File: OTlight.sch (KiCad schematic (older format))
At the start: 51 parts

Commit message: Everything Connected
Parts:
- removed P?: Vin, Pin_Headers:Pin_Header_Straight_1x02, symbol CONN_01X02
- removed P?: Vout, Pin_Headers:Pin_Header_Straight_1x02, symbol CONN_01X02
- added P1: CONN_01X01, symbol CONN_01X01
- gave numbers to parts that had none: 49
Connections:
- wire segments 228 -> 239
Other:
- note added: "ESPain"
- moved on the sheet: C1, C4, C6, R7

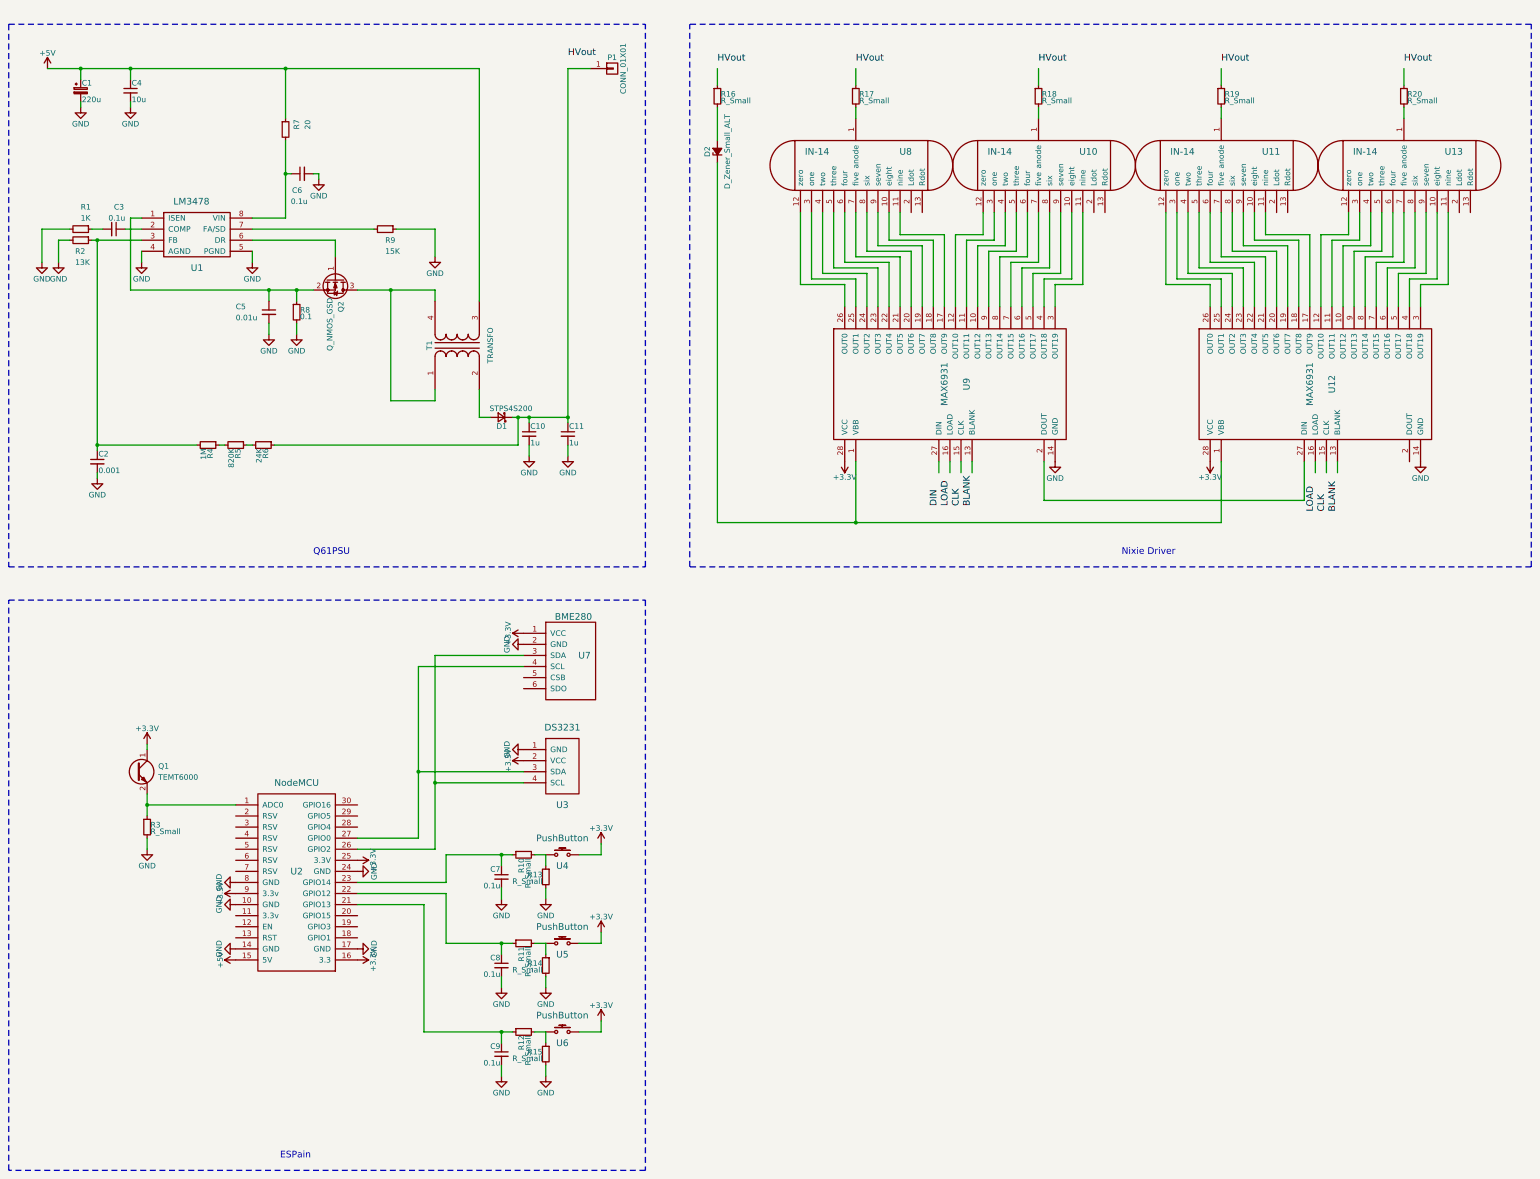
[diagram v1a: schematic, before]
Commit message: Touch up + added I2C Pullups
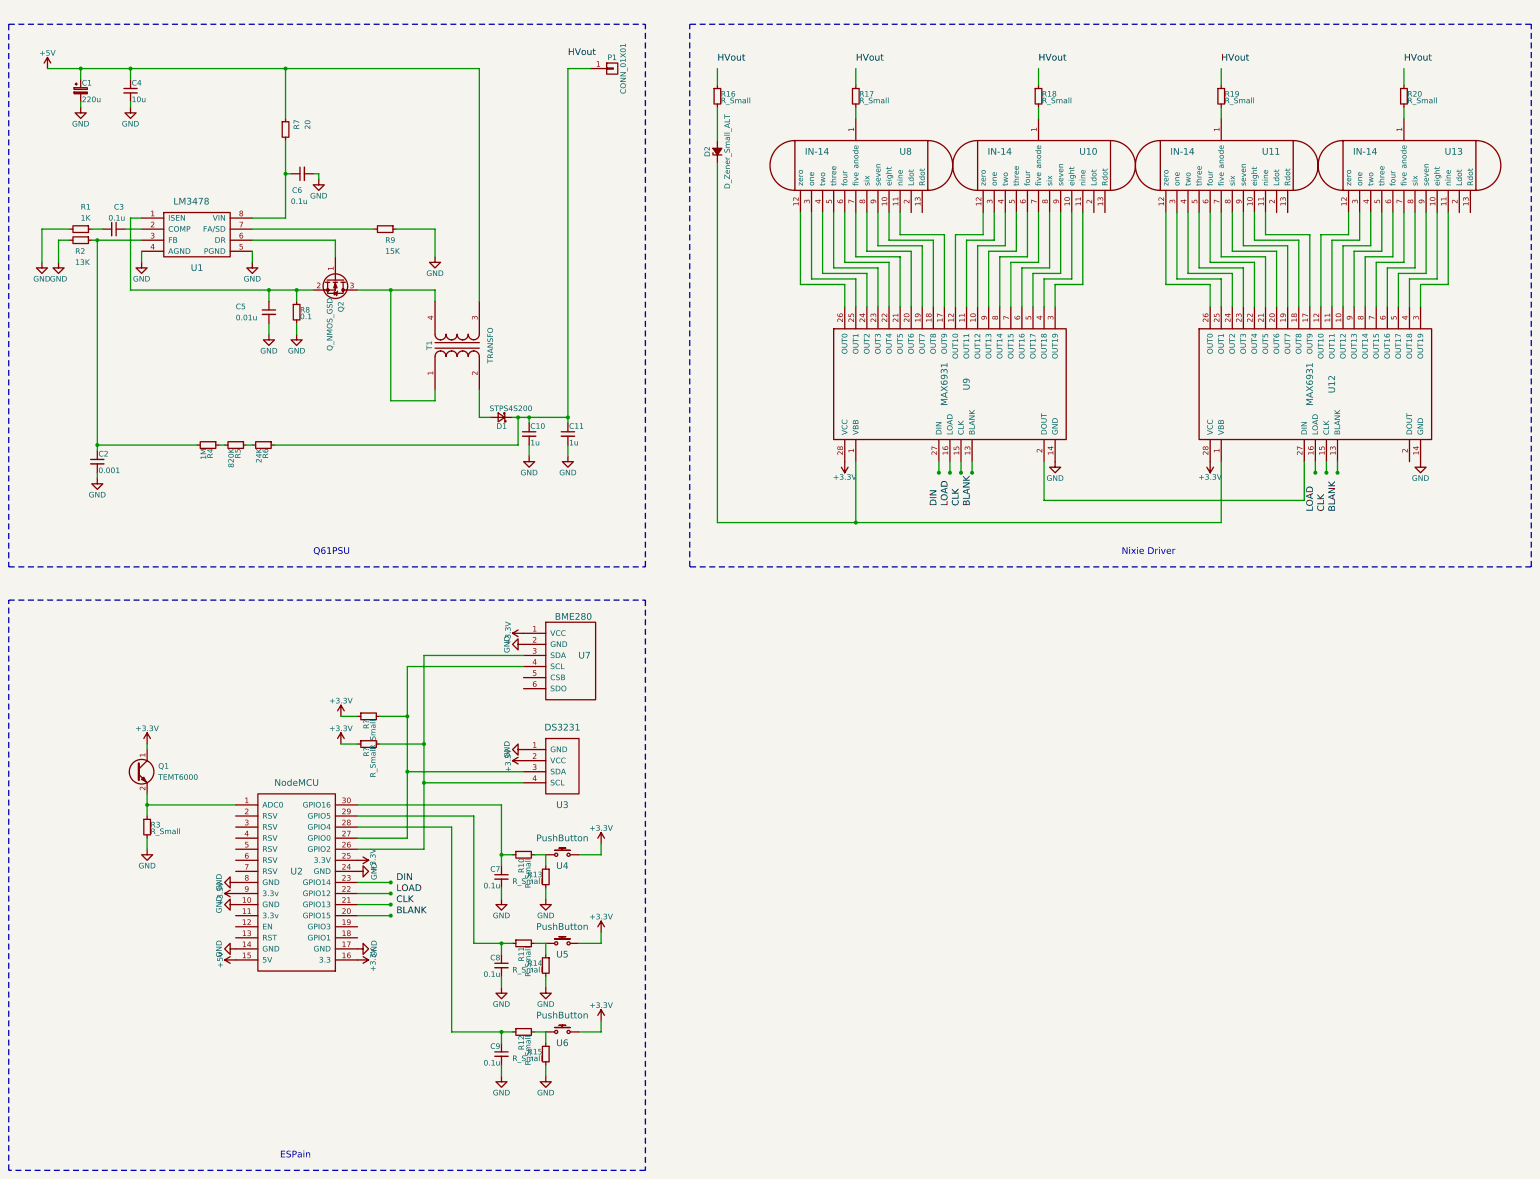
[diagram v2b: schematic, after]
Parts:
- added R? (x2): R_Small, symbol R_Small
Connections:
- wire segments 239 -> 267
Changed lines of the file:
@@
 LIBS:contrib
 LIBS:valves
+LIBS:ESP8266
 LIBS:bambouLab
-LIBS:ESP8266
 LIBS:OTlight-cache
 EELAYER 25 0
@@
 encoding utf-8
 Sheet 1 1
-Title ""
-Date ""
-Rev ""
-Comp ""
+Title "OT;Light"
+Date "2017-01-21"
+Rev "0.1"
+Comp "bambou;Lab"
 Comment1 ""
 Comment2 ""
@@
 Connection ~ 1800 1050
 Wire Wire Line
-	3200 1700 3200 2400
+	3200 1700 3200 2000
+Wire Wire Line
+	3200 2000 3200 2400
 Wire Wire Line
 	3200 2000 3250 2000
@@
 	3650 2600 3650 2750
 Wire Wire Line
-	3850 3050 4550 3050
+	3850 3050 4150 3050
+Wire Wire Line
+	4150 3050 4550 3050
 Wire Wire Line
 	4150 3050 4150 4050
@@
 Connection ~ 4150 3050
 Wire Wire Line
-	1800 3050 3450 3050
+	1800 3050 3050 3050
+Wire Wire Line
+	3050 3050 3300 3050
+Wire Wire Line
+	3300 3050 3450 3050
 Wire Wire Line
 	3050 3050 3050 3150
@@
 	1550 2500 1450 2500
 Wire Wire Line
-	1450 2600 1900 2600
+	1450 2600 1500 2600
+Wire Wire Line
+	1500 2600 1900 2600
 Wire Wire Line
 	1250 2600 1150 2600
@@
 	5950 1050 5750 1050
 Wire Wire Line
-	5750 1050 5750 4250
-Wire Wire Line
-	5250 4200 5750 4200
+	5750 1050 5750 4200
+Wire Wire Line
+	5750 4200 5750 4250
+Wire Wire Line
+	5250 4200 5300 4200
+Wire Wire Line
+	5300 4200 5400 4200
+Wire Wire Line
+	5400 4200 5750 4200
 Wire Wire Line
 	4950 4200 5050 4200
@@
 Connection ~ 5400 4200
 Wire Wire Line
-	1500 2600 1500 4500
+	1500 2600 1500 4450
+Wire Wire Line
+	1500 4450 1500 4500
 Connection ~ 1500 2600
 Wire Wire Line
@@
 	7100 1900 7100 5150
 Wire Wire Line
-	7100 5150 11650 5150
+	7100 5150 8350 5150
+Wire Wire Line
+	8350 5150 11650 5150
 Wire Wire Line
 	8350 5150 8350 4600
@@
 	2750 7700 1950 7700
 Wire Wire Line
-	1950 7600 1950 7800
+	1950 7600 1950 7700
+Wire Wire Line
+	1950 7700 1950 7800
 $Comp
 L R_Small R3
@@
 	5550 8450 5550 8550
 Wire Wire Line
-	4650 8150 5250 8150
+	5150 7700 5150 8150
 Wire Wire Line
 	5150 8150 5150 8250
@@
 	5550 9250 5550 9350
 Wire Wire Line
-	4650 8950 5250 8950
-Wire Wire Line
 	5150 8950 5150 9050
 Wire Wire Line
@@
 	5550 10050 5550 10150
 Wire Wire Line
-	4450 9750 5250 9750
-Wire Wire Line
 	5150 9750 5150 9850
 Wire Wire Line
@@
 	3200 2400 2900 2400
 Wire Wire Line
-	4950 1050 1050 1050
+	1050 1050 1350 1050
+Wire Wire Line
+	1350 1050 1800 1050
+Wire Wire Line
+	1800 1050 3200 1050
+Wire Wire Line
+	3200 1050 4950 1050
 Text Notes 3150 10900 0    60   ~ 0
 ESPain
 Wire Wire Line
-	3850 8000 4400 8000
-Wire Wire Line
-	4400 8000 4400 6450
-Wire Wire Line
-	4400 6450 5350 6450
-Wire Wire Line
-	3850 8100 4550 8100
-Wire Wire Line
-	4550 8100 4550 6350
-Wire Wire Line
-	4550 6350 5350 6350
-Wire Wire Line
-	5350 7400 4400 7400
-Connection ~ 4400 7400
-Wire Wire Line
-	5350 7500 4550 7500
-Connection ~ 4550 7500
-Wire Wire Line
-	3850 8400 4650 8400
-Wire Wire Line
-	4650 8400 4650 8150
+	4300 8000 3850 8000
+Wire Wire Line
+	4300 6450 4300 6900
+Wire Wire Line
+	4300 6900 4300 7400
+Wire Wire Line
+	4300 7400 4300 8000
+Wire Wire Line
+	4300 6450 5350 6450
+Wire Wire Line
+	4450 8100 3850 8100
+Wire Wire Line
+	4450 6350 4450 7150
+Wire Wire Line
+	4450 7150 4450 7500
+Wire Wire Line
+	4450 7500 4450 8100
+Wire Wire Line
+	4450 6350 5350 6350
+Wire Wire Line
+	5350 7400 4300 7400
+Connection ~ 4300 7400
+Wire Wire Line
+	5350 7500 4450 7500
+Connection ~ 4450 7500
 Connection ~ 5150 8150
-Wire Wire Line
-	3850 8500 4650 8500
-Wire Wire Line
-	4650 8500 4650 8950
 Connection ~ 5150 8950
-Wire Wire Line
-	3850 8600 4450 8600
-Wire Wire Line
-	4450 8600 4450 9750
 Connection ~ 5150 9750
+Wire Wire Line
+	3850 7700 5150 7700
+Wire Wire Line
+	5150 8150 5250 8150
+Wire Wire Line
+	3850 7800 4900 7800
+Wire Wire Line
+	3850 7900 4700 7900
+Wire Wire Line
+	4900 8950 5150 8950
+Wire Wire Line
+	5150 8950 5250 8950
+Wire Wire Line
+	4900 7800 4900 8950
+Wire Wire Line
+	3850 8400 4150 8400
+Wire Wire Line
+	3850 8500 4150 8500
+Wire Wire Line
+	3850 8600 4150 8600
+Wire Wire Line
+	3850 8700 4150 8700
+Text Label 4200 8400 0    60   ~ 0
+DIN
+Text Label 4200 8500 0    60   ~ 0
+LOAD
+Text Label 4200 8600 0    60   ~ 0
+CLK
+Text Label 4200 8700 0    60   ~ 0
+BLANK
+Connection ~ 4150 8400
+Connection ~ 4150 8500
+Connection ~ 4150 8600
+Connection ~ 4150 8700
+Connection ~ 9100 4700
+Connection ~ 9200 4700
+Connection ~ 9300 4700
+Connection ~ 9400 4700
+Connection ~ 12500 4700
+Connection ~ 12600 4700
+Connection ~ 12700 4700
+Wire Wire Line
+	4700 7900 4700 9750
+Wire Wire Line
+	4700 9750 5150 9750
+Wire Wire Line
+	5150 9750 5250 9750
+$Comp
+L +3.3V #PWR?
+U 1 1 5884F76D
+P 3700 6900
+F 0 "#PWR?" H 3700 6750 50  0001 C CNN
+F 1 "+3.3V" H 3700 7040 50  0000 C CNN
+F 2 "" H 3700 6900 50  0000 C CNN
+F 3 "" H 3700 6900 50  0000 C CNN
+	1    3700 6900
+	-1   0    0    -1
+$EndComp
+$Comp
+L +3.3V #PWR?
+U 1 1 5884F80E
+P 3700 7150
+F 0 "#PWR?" H 3700 7000 50  0001 C CNN
+F 1 "+3.3V" H 3700 7290 50  0000 C CNN
+F 2 "" H 3700 7150 50  0000 C CNN
+F 3 "" H 3700 7150 50  0000 C CNN
+	1    3700 7150
+	-1   0    0    -1
+$EndComp
+$Comp
+L R_Small R?
+U 1 1 5884F8AF
+P 3950 6900
+F 0 "R?" H 3980 6920 50  0000 L CNN
+F 1 "R_Small" H 3980 6860 50  0000 L CNN
+F 2 "" H 3950 6900 50  0000 C CNN
+F 3 "" H 3950 6900 50  0000 C CNN
+	1    3950 6900
+	0    -1   1    0
+$EndComp
+$Comp
+L R_Small R?
+U 1 1 5884F982
+P 3950 7150
+F 0 "R?" H 3980 7170 50  0000 L CNN
+F 1 "R_Small" H 3980 7110 50  0000 L CNN
+F 2 "" H 3950 7150 50  0000 C CNN
+F 3 "" H 3950 7150 50  0000 C CNN
+	1    3950 7150
+	0    -1   1    0
+$EndComp
+Wire Wire Line
+	3700 6900 3850 6900
+Wire Wire Line
+	3850 7150 3700 7150
+Wire Wire Line
+	4050 6900 4300 6900
+Connection ~ 4300 6900
+Wire Wire Line
+	4050 7150 4450 7150
+Connection ~ 4450 7150
 $EndSCHEMATC

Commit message: Schematic Update
changelog:
- Linked labels
- Added MAXIM6920 to rout the dot
- Set values to passive components
- Cosmetic changes
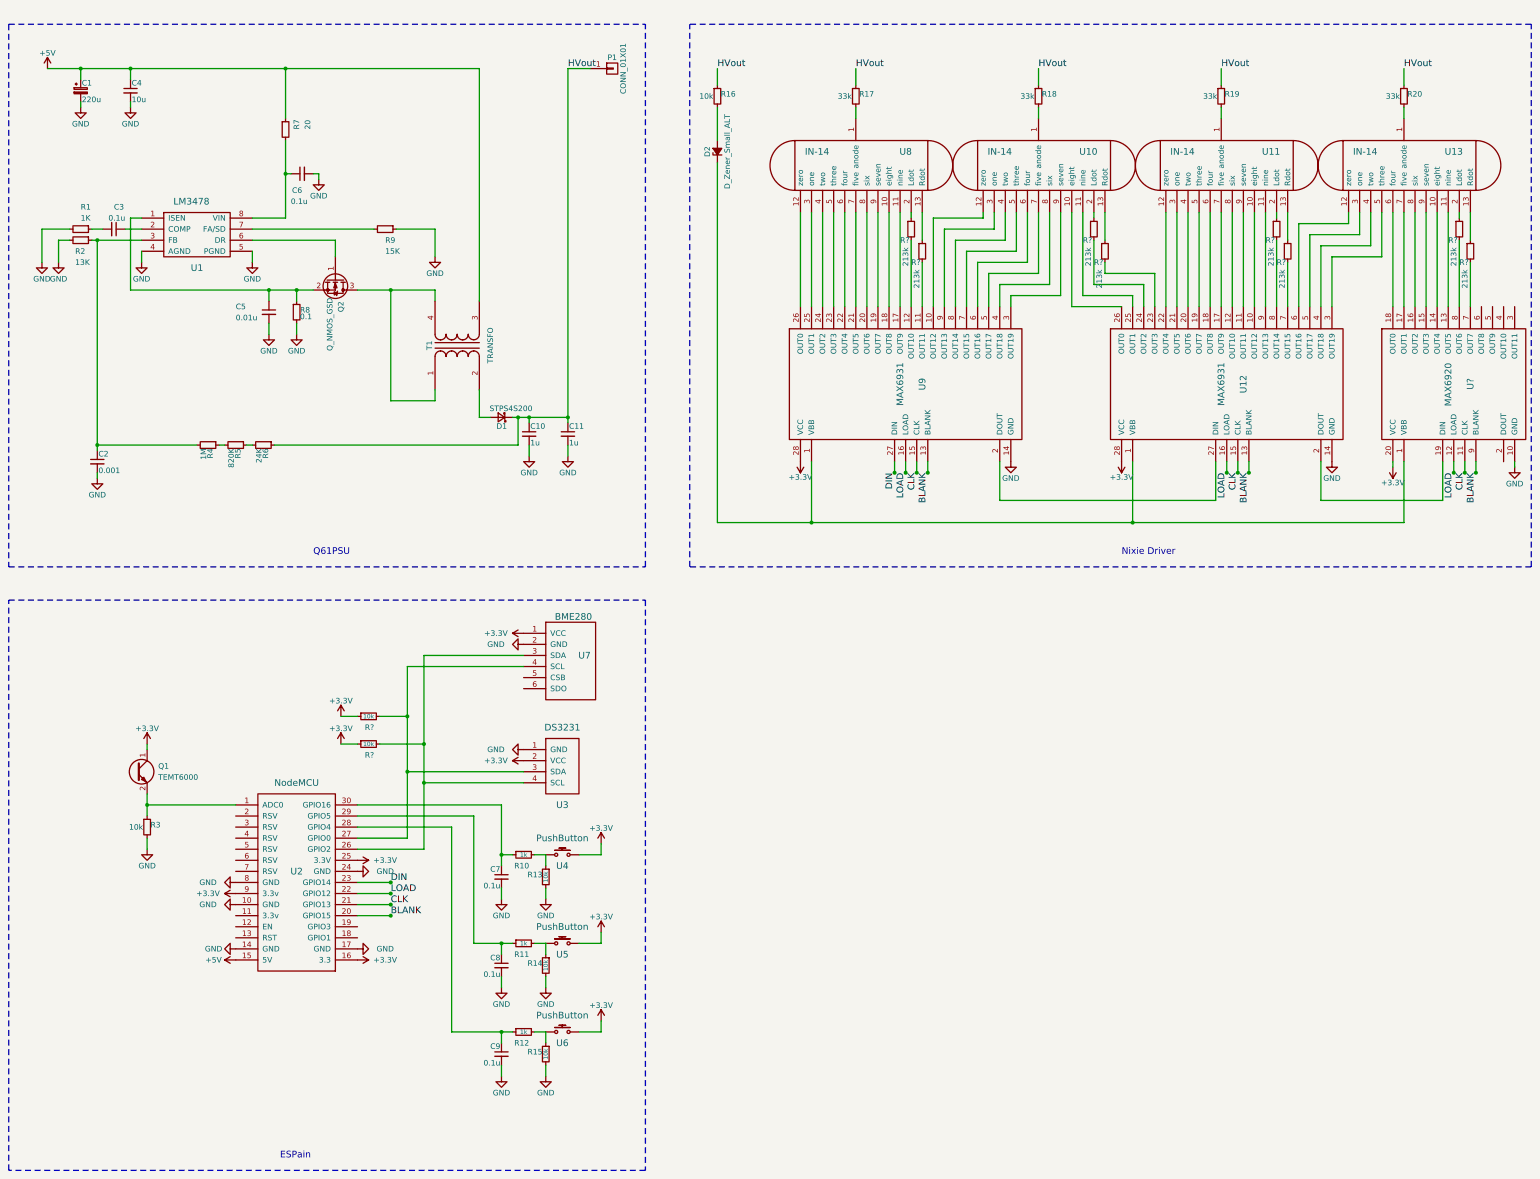
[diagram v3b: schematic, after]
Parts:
- added R? (x8): R_Small, symbol R_Small
- added U?: MAX6920, symbol MAX6920
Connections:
- net +3V3: now also U?.20 (VCC)
- net BLANK: now also U12.13 (BLANK), U2.20 (GPIO15), U9.13 (BLANK), U?.9 (BLANK)
- net CLK: now also U12.15 (CLK), U2.21 (GPIO13), U9.15 (CLK), U?.11 (CLK)
- net DIN: now also U2.23 (GPIO14), U9.27 (DIN)
- net GND: now also U?.10 (GND)
- net HVout: now also C10.1, C11.1, D1.1 (K), P1.1 (P1), R16.1, R17.1, R18.1, R19.1, R20.1, R6.1
- net LOAD: now also U12.16 (LOAD), U2.22 (GPIO12), U9.16 (LOAD), U?.12 (LOAD)
- net at U8.13 (Rdot): now also R?.1
- net at U8.2 (Ldot): now also R?.1
- net at U10.10 (eight): now also U12.26 (OUT0); no longer U9.4 (OUT18)
- net at U10.11 (nine): now also U12.25 (OUT1); no longer U9.3 (OUT19)
- net at U10.12 (zero): now also U9.10 (OUT12); no longer U9.12 (OUT10)
- net at U10.13 (Rdot): now also R?.1
- net at U10.2 (Ldot): now also R?.1
- net at U10.3 (one): now also U9.9 (OUT13); no longer U9.11 (OUT11)
- net at U10.4 (two): now also U9.8 (OUT14); no longer U9.10 (OUT12)
- net at U10.5 (three): now also U9.7 (OUT15); no longer U9.9 (OUT13)
- net at U10.6 (four): now also U9.6 (OUT16); no longer U9.8 (OUT14)
- net at U10.7 (five): now also U9.5 (OUT17); no longer U9.7 (OUT15)
- net at U10.8 (six): now also U9.4 (OUT18); no longer U9.6 (OUT16)
- net at U10.9 (seven): now also U9.3 (OUT19); no longer U9.5 (OUT17)
- net at U11.10 (eight): now also U12.10 (OUT12); no longer U12.18 (OUT8)
- net at U11.11 (nine): now also U12.9 (OUT13); no longer U12.17 (OUT9)
- net at U11.12 (zero): now also U12.22 (OUT4); no longer U12.26 (OUT0)
- net at U11.13 (Rdot): now also R?.1
- net at U11.2 (Ldot): now also R?.1
- net at U11.3 (one): now also U12.21 (OUT5); no longer U12.25 (OUT1)
- net at U11.4 (two): now also U12.20 (OUT6); no longer U12.24 (OUT2)
- net at U11.5 (three): now also U12.19 (OUT7); no longer U12.23 (OUT3)
- net at U11.6 (four): now also U12.18 (OUT8); no longer U12.22 (OUT4)
- net at U11.7 (five): now also U12.17 (OUT9); no longer U12.21 (OUT5)
- net at U11.8 (six): now also U12.12 (OUT10); no longer U12.20 (OUT6)
- net at U11.9 (seven): now also U12.11 (OUT11); no longer U12.19 (OUT7)
- net at U13.10 (eight): now also U?.14 (OUT4); no longer U12.4 (OUT18)
- net at U13.11 (nine): now also U?.13 (OUT5); no longer U12.3 (OUT19)
- net at U13.12 (zero): now also U12.6 (OUT16); no longer U12.12 (OUT10)
- net at U13.13 (Rdot): now also R?.1
- net at U13.2 (Ldot): now also R?.1
- net at U13.3 (one): now also U12.5 (OUT17); no longer U12.11 (OUT11)
- net at U13.4 (two): now also U12.4 (OUT18); no longer U12.10 (OUT12)
- net at U13.5 (three): now also U12.3 (OUT19); no longer U12.9 (OUT13)
- net at U13.6 (four): now also U?.18 (OUT0); no longer U12.8 (OUT14)
- net at U13.7 (five): now also U?.17 (OUT1); no longer U12.7 (OUT15)
- net at U13.8 (six): now also U?.16 (OUT2); no longer U12.6 (OUT16)
- net at U13.9 (seven): now also U?.15 (OUT3); no longer U12.5 (OUT17)
- net at D2.1 (K), U12.1 (VBB), U9.1 (VBB): now also U?.1 (VBB)
- net at U12.2 (DOUT): now also U?.19 (DIN)
- new net: R?.2, U9.11 (OUT11)
- new net: R?.2, U9.12 (OUT10)
- new net: R?.2, U12.23 (OUT3)
- new net: R?.2, U12.24 (OUT2)
- new net: R?.2, U12.7 (OUT15)
- new net: R?.2, U12.8 (OUT14)
- new net: R?.2, U?.7 (OUT7)
- new net: R?.2, U?.8 (OUT6)
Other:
- moved on the sheet: U12, U9
